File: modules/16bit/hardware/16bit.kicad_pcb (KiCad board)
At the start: 4 copper layers, 29 x 110 mm, 99 parts, among them J1 PJ301M-12, J2 PJ301M-12, J3 PJ301M-12, J4 PJ301M-12, J5 PJ301M-12, J6 Eurorack_2x5, J7 USB-C, Q1 MMBT3904, SW1 MODE, SW2 BOOT, SW3 RUN, U1 RP2350A, U2 W25Q128JVS, U3 APS6404L-3SQR-SN, U4 PT8211, U5 TL074, U6 MCP6002, U7 TL072, U8 AMS1117-5.0, U9 AMS1117-3.3, Y1 12MHz

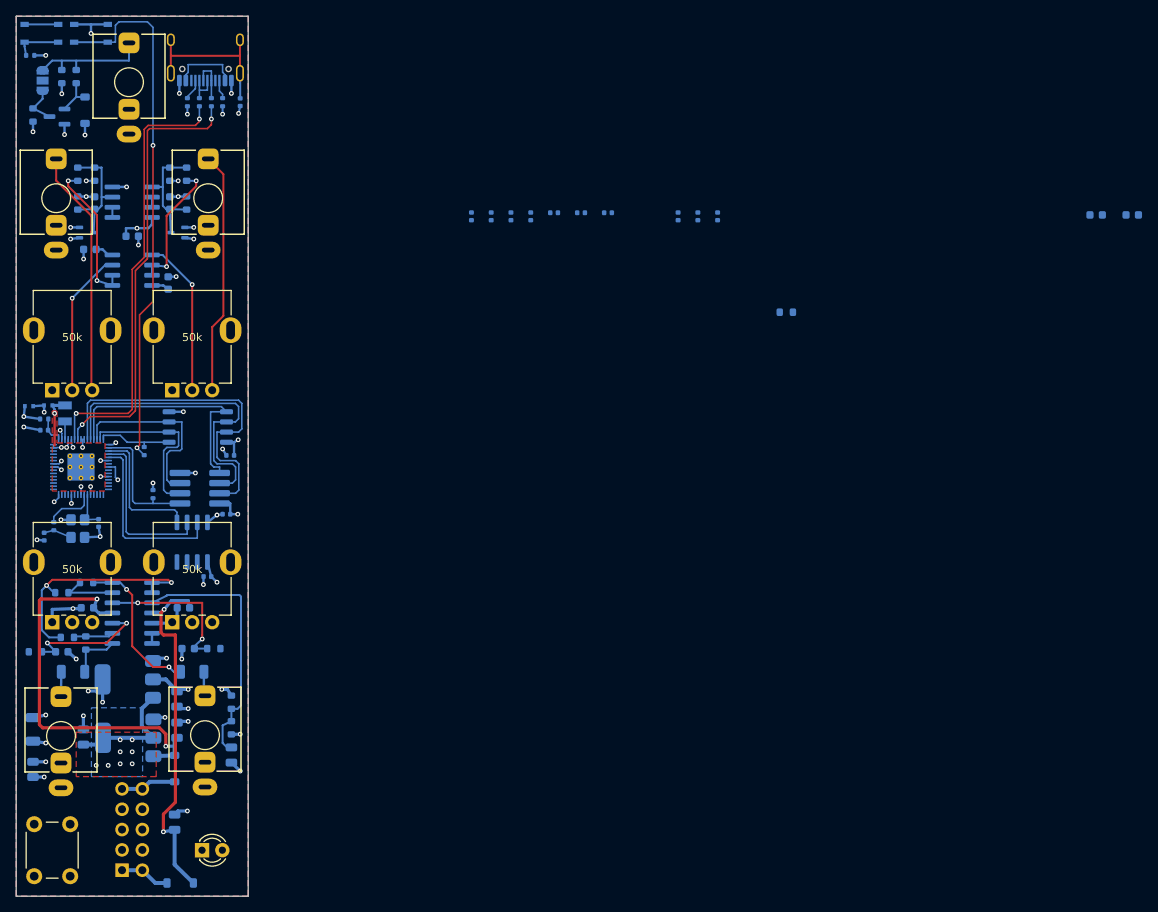
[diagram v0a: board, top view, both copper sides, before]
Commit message: Added better 16bit routing setup.
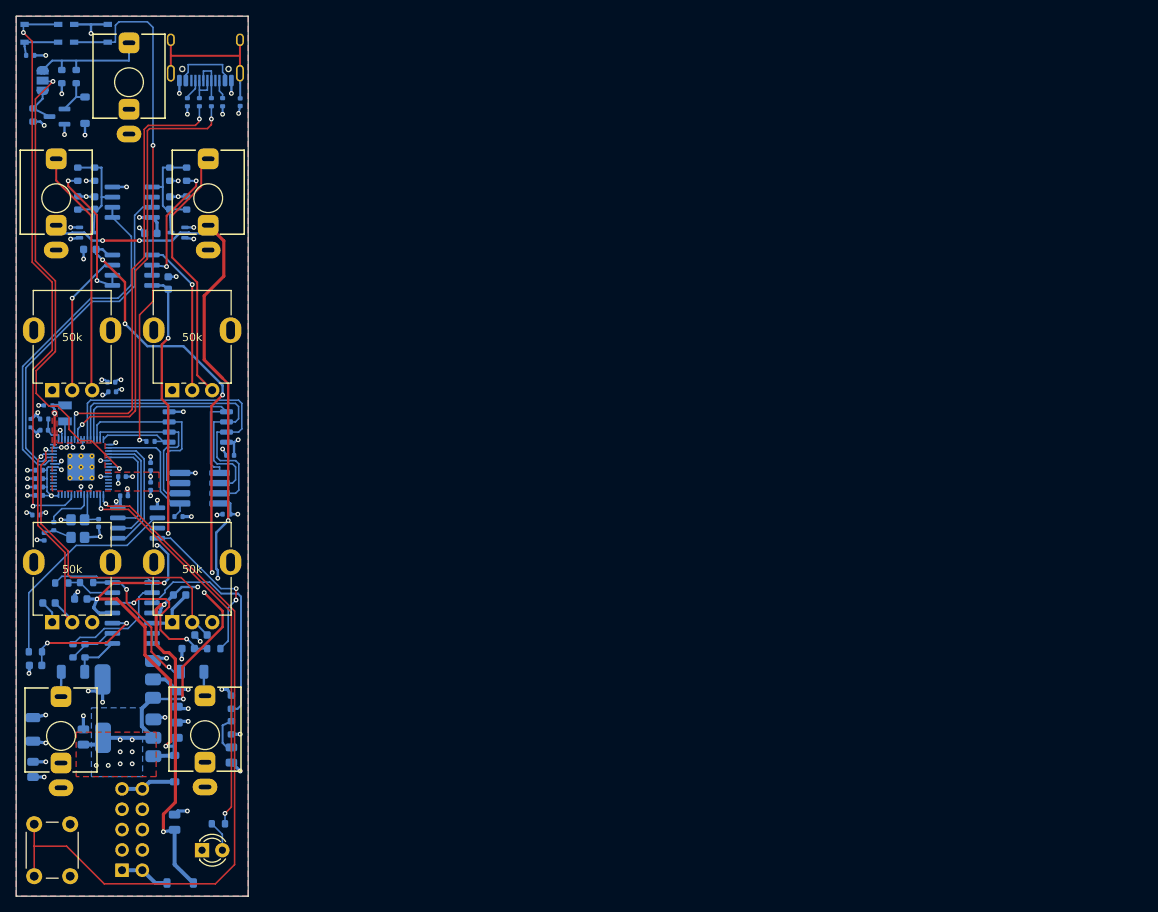
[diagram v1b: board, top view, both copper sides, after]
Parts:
- moved C30 139.6 mm to (104.6, 132.6)
- moved C31 127.7 mm to (123.6, 136.6)
- moved R20 95.5 mm to (125.8, 160.2)
- moved C16 81.2 mm to (113.7, 116.8), turned to 0 degrees
- moved C15 76.3 mm to (117.3, 118.0), turned to -90 degrees
- moved C9 73.4 mm to (103.3, 119.2)
- moved C14 73.0 mm to (117.3, 115.5)
- moved C8 70.2 mm to (103.3, 118.1), turned to 180 degrees
- moved C7 67.5 mm to (103.3, 117.0), turned to 180 degrees
- moved C5 66.0 mm to (103.0, 121.6), turned to 180 degrees
- moved C11 65.9 mm to (112.5, 106.2)
- moved C6 64.8 mm to (103.3, 116.0), turned to 180 degrees
- moved C10 62.4 mm to (112.4, 105.0)
- moved C33 14.5 mm to (114.0, 119.2)
- moved U4 7.23 mm to (115.7, 122.6), turned to 0 degrees
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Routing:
- net +5V: track 14.9 -> 106.3 mm, vias 8 -> 14
- net /BUTTON: track 0.00 -> 89.1 mm, vias 0 -> 1
- net /RUN: track 5.31 -> 72.8 mm, vias 1 -> 2
- net /MIDI_RX: track 2.59 -> 59.9 mm, vias 1 -> 2
- net -12V_F: track 47.7 -> 104.2 mm, vias 2 -> 7
- net /LED: track 0.00 -> 50.2 mm, vias 0 -> 2
- net /CV2_ADC: track 1.27 -> 44.9 mm
- net /CV1_ADC: track 1.27 -> 43.7 mm
- net /POT4: track 0.00 -> 40.8 mm, vias 0 -> 1
- net +12V_F: track 52.7 -> 85.4 mm, vias 2 -> 6
- net /POT3: track 0.00 -> 27.6 mm, vias 0 -> 1
- net /DAC_L: track 0.00 -> 27.3 mm
- net /DAC_R: track 0.00 -> 20.8 mm, vias 0 -> 2
- net GND: track 72.4 -> 82.2 mm, vias 41 -> 52
- net /I2S_DIN: track 22.8 -> 13.2 mm
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
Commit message: Add JLCPCB export for 16bit
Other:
- board text added: "BOOT"
- board text added: "D=DIRECT"
- board text added: "MIDI JP1"
- board text added: "P=PROT"
- board text added: "RESET"
